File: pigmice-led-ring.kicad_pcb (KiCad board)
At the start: 2 copper layers, 46 x 51 mm, 46 parts, among them J1 Conn_01x02_Female, J2 Conn_01x03_Female, U1 LMR62014XMF

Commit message: Cleanup voltage regulator circuit spacing
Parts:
- moved C1 1.38 mm to (78.6, 99.3)
- moved CF1 1.34 mm to (79.6, 105.8)
- moved U1 1.18 mm to (78.8, 102.0)
- moved C2 1.17 mm to (75.2, 103.6)
- moved R2 1.15 mm to (81.6, 105.2)
- moved R3 1.13 mm to (81.6, 101.8)
- moved D1 1.11 mm to (74.5, 101.5)
- moved R1 1.11 mm to (77.8, 105.8)
- moved L1 0.40 mm to (74.6, 98.2)
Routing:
- net GND: track 17.7 -> 8.85 mm
- net /Vled: track 10.3 -> 7.52 mm
- net /PWM: track 15.3 -> 16.4 mm
- net Net-(D1-Pad2): track 7.42 -> 6.85 mm

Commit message: Add sponsor logos
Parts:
- added G***: LOGO, led-ring:oshpark_logo, B.Cu at (84.0, 99.5)
- added G***: LOGO, led-ring:terrazign_logo, B.Cu at (107.0, 70.5)
- added G***: LOGO, led-ring:daimler_logo, B.Cu at (79.0, 60.0)
- added G***: LOGO, led-ring:flir_logo, B.Cu at (102.0, 61.0)
- added G***: LOGO, led-ring:frc_logo, B.Cu at (90.0, 62.0)
- added G***: LOGO, led-ring:o_edu_logo, B.Cu at (108.0, 80.0)
- added G***: LOGO, led-ring:oshw_logo, B.Cu at (96.5, 99.0)
- added G***: LOGO, led-ring:sw_logo, B.Cu at (76.5, 65.0)
- added G***: LOGO, led-ring:urs_electronics_logo, B.Cu at (72.0, 80.0)
- added G***: LOGO, led-ring:dw_fritz_logo, B.Cu at (107.0, 89.0)
- added G***: LOGO, led-ring:true_value_logo, B.Cu at (73.0, 89.0)
- added G***: LOGO, led-ring:boeing_logo, B.Cu at (73.0, 70.0)
- added G***: LOGO, led-ring:te_logo, B.Cu at (104.0, 65.0)

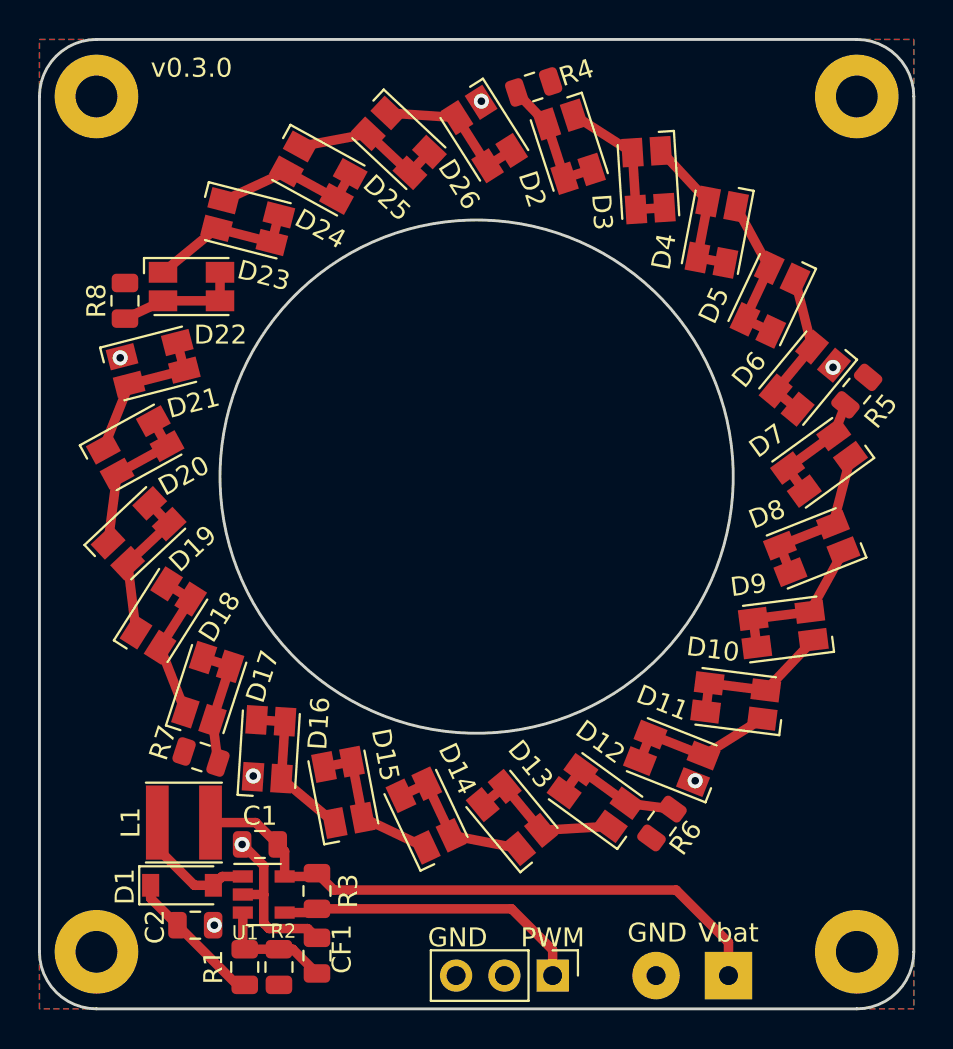
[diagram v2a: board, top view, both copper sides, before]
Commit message: Move LED vias out of underneath pad
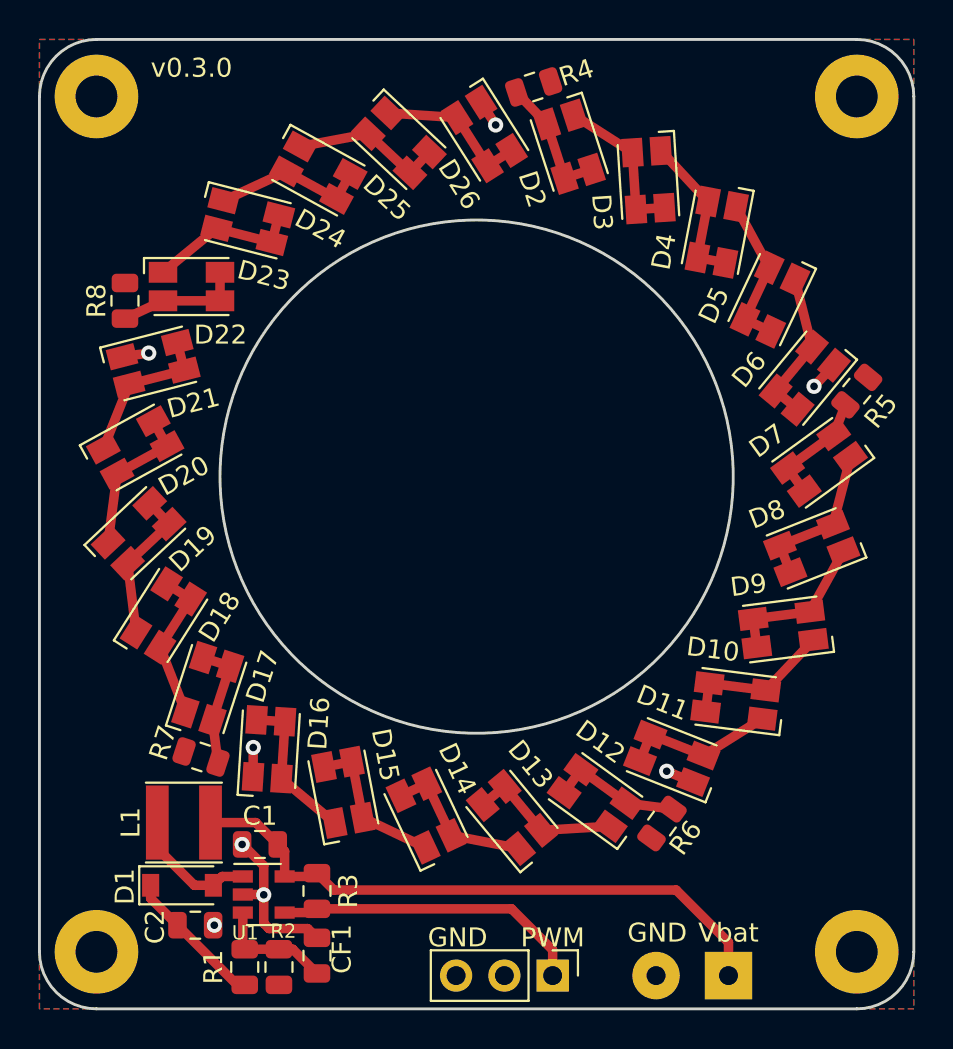
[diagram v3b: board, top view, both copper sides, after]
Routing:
- net GND: track 8.85 -> 16.3 mm, vias 7 -> 8
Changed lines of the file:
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@@
     (thickness 1.6)
     (drawings 14)
-    (tracks 122)
+    (tracks 132)
     (zones 0)
     (modules 59)
@@
     (34 B.Paste user)
     (35 F.Paste user)
-    (36 B.SilkS user)
+    (36 B.SilkS user hide)
     (37 F.SilkS user)
     (38 B.Mask user)
@@
     (via_min_size 0.4)
     (via_min_drill 0.3)
+    (user_via 0.6 0.3)
     (uvia_size 0.3)
     (uvia_drill 0.1)
@@
   (gr_arc (start 110 60) (end 113 60) (angle -90) (layer Edge.Cuts) (width 0.15))
   (gr_arc (start 70 60) (end 70 57) (angle -90) (layer Edge.Cuts) (width 0.15))
+  (via (at 76.2 103.6) (size 0.8) (drill 0.4) (layers F.Cu B.Cu) (net 2))
   (segment (start 81.402661 102.934839) (end 81.6 102.7375) (width 0.5) (layer F.Cu) (net 1))
   (segment (start 79.9 102.934839) (end 81.402661 102.934839) (width 0.5) (layer F.Cu) (net 1))
@@
   (segment (start 91.8375 102.7375) (end 81.6 102.7375) (width 0.5) (layer F.Cu) (net 1))
   (segment (start 94 104.9) (end 91.8375 102.7375) (width 0.5) (layer F.Cu) (net 1))
-  (via (at 76.2 103.6) (size 0.8) (drill 0.4) (layers F.Cu B.Cu) (net 2))
-  (via (at 78.25 95.75) (size 0.8) (drill 0.4) (layers F.Cu B.Cu) (net 2))
-  (via (at 108.75 74.25) (size 0.8) (drill 0.4) (layers F.Cu B.Cu) (net 2))
-  (via (at 101.5 96) (size 0.8) (drill 0.4) (layers F.Cu B.Cu) (net 2))
-  (via (at 71.25 73.75) (size 0.8) (drill 0.4) (layers F.Cu B.Cu) (net 2))
-  (via (at 90.25 60.25) (size 0.8) (drill 0.4) (layers F.Cu B.Cu) (net 2))
+  (via (at 78.25 94.25) (size 0.8) (drill 0.4) (layers F.Cu B.Cu) (net 2))
+  (via (at 107.75 75.25) (size 0.8) (drill 0.4) (layers F.Cu B.Cu) (net 2))
+  (via (at 100 95.5) (size 0.8) (drill 0.4) (layers F.Cu B.Cu) (net 2))
+  (via (at 72.75 73.5) (size 0.8) (drill 0.4) (layers F.Cu B.Cu) (net 2))
+  (via (at 91 61.5) (size 0.8) (drill 0.4) (layers F.Cu B.Cu) (net 2))
   (segment (start 77.680163 99.35) (end 78.8 100.469837) (width 0.5) (layer F.Cu) (net 2))
   (segment (start 77.6625 99.35) (end 77.6625 99.35) (width 0.5) (layer F.Cu) (net 2))
@@
   (segment (start 81.114473 103.776973) (end 81.6 104.2625) (width 0.5) (layer F.Cu) (net 2))
   (segment (start 78.8 103.499841) (end 79.077132 103.776973) (width 0.5) (layer F.Cu) (net 2))
+  (segment (start 78.8 102) (end 78.8 102) (width 0.5) (layer F.Cu) (net 2))
+  (segment (start 77.6625 99.35) (end 77.6625 99.35) (width 0.5) (layer F.Cu) (net 2))
+  (segment (start 91 61.5) (end 90.235383 60.308451) (width 0.5) (layer F.Cu) (net 2))
+  (segment (start 107.75 75.25) (end 108.800513 74.138839) (width 0.5) (layer F.Cu) (net 2))
+  (segment (start 100 95.5) (end 101.383973 96.069152) (width 0.5) (layer F.Cu) (net 2))
+  (segment (start 78.25 94.25) (end 78.235169 95.792443) (width 0.5) (layer F.Cu) (net 2))
+  (segment (start 72.75 73.5) (end 71.344962 73.691114) (width 0.5) (layer F.Cu) (net 2))
+  (segment (start 78.8 102) (end 78.8 102) (width 0.5) (layer F.Cu) (net 2))
+  (segment (start 78.8 102) (end 78.8 102) (width 0.5) (layer F.Cu) (net 2))
   (segment (start 78.8 102) (end 78.8 103.499841) (width 0.5) (layer F.Cu) (net 2))
+  (via (at 78.8 102) (size 0.8) (drill 0.4) (layers F.Cu B.Cu) (net 2))
   (segment (start 77.6625 99.35) (end 77.680163 99.35) (width 0.5) (layer F.Cu) (net 2))
   (via (at 77.6625 99.35) (size 0.8) (drill 0.4) (layers F.Cu B.Cu) (net 2))
@@
   (segment (start 103.25 104.50032) (end 100.49968 101.75) (width 0.5) (layer F.Cu) (net 12))
   (segment (start 103.25 106.25) (end 103.25 104.50032) (width 0.5) (layer F.Cu) (net 12))
-  (segment (start 78.3875 98.2) (end 79.5375 99.35) (width 0.5) (layer F.Cu) (net 12))
-  (segment (start 76 98.2) (end 78.3875 98.2) (width 0.5) (layer F.Cu) (net 12))
   (segment (start 79.9 99.7125) (end 79.5375 99.35) (width 0.5) (layer F.Cu) (net 12))
   (segment (start 79.9 101.034839) (end 79.9 99.7125) (width 0.5) (layer F.Cu) (net 12))
@@
   (segment (start 82.4875 101.75) (end 100.49968 101.75) (width 0.5) (layer F.Cu) (net 12))
   (segment (start 81.6 100.8625) (end 82.4875 101.75) (width 0.5) (layer F.Cu) (net 12))
+  (segment (start 78.3875 98.2) (end 79.5375 99.35) (width 0.5) (layer F.Cu) (net 12))
+  (segment (start 76 98.2) (end 78.3875 98.2) (width 0.5) (layer F.Cu) (net 12))
   (segment (start 103.089234 68.753471) (end 101.615805 68.472399) (width 0.5) (layer F.Cu) (net 14))
   (segment (start 101.615805 68.472399) (end 102.17795 65.525537) (width 0.5) (layer F.Cu) (net 14))

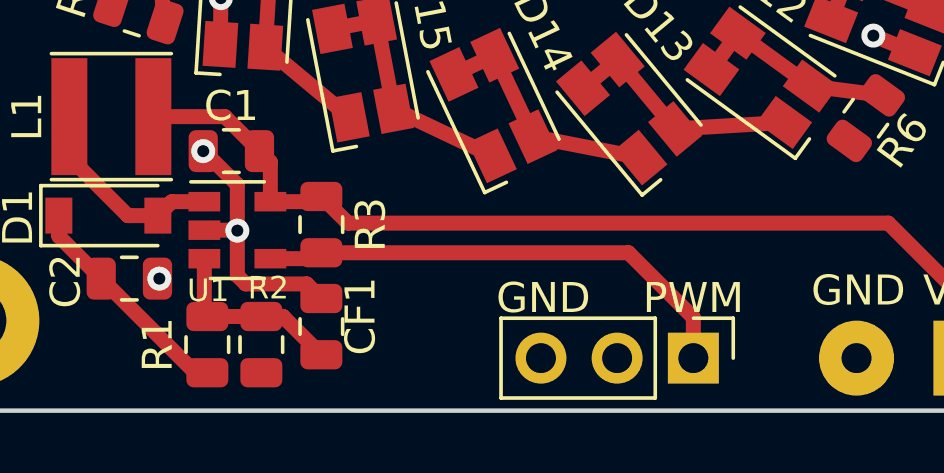
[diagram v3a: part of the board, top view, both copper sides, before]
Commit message: Fix R2/CF1 labels
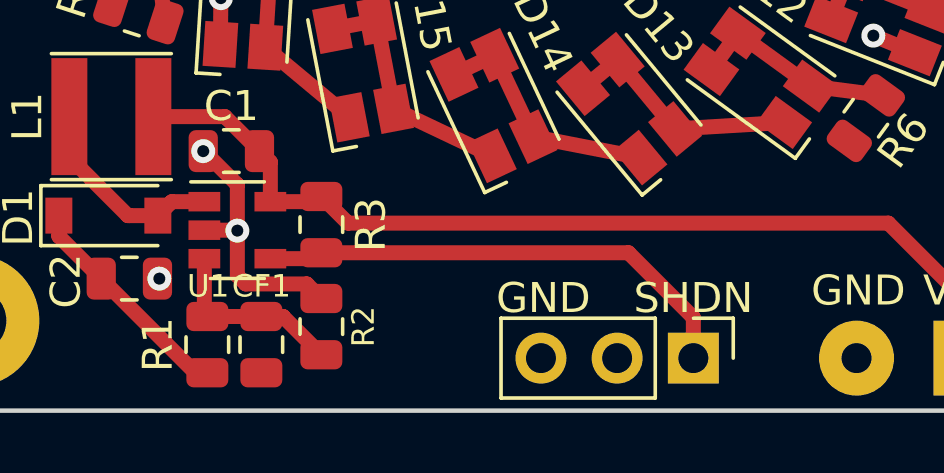
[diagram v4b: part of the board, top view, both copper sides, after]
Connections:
- net /PWM renamed /SHDN
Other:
- board text added: "SHDN"
- board text removed: "PWM"

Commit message: Center URS logo better
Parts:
- moved G*** 0.25 mm to (71.8, 80.0)
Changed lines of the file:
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@@
     (34 B.Paste user)
     (35 F.Paste user)
-    (36 B.SilkS user hide)
+    (36 B.SilkS user)
     (37 F.SilkS user)
     (38 B.Mask user)
@@
   )
   (module led-ring:urs_electronics_logo (layer B.Cu)
-    (at 72 80 180)
+    (at 71.75 80 180)
     (fp_text reference G*** (at 0 0) (layer B.SilkS) hide
       (effects (font (size 1.524 1.524) (thickness 0.3)) (justify mirror))
@@
   (gr_arc (start 110 60) (end 113 60) (angle -90) (layer Edge.Cuts) (width 0.15))
   (gr_arc (start 70 60) (end 70 57) (angle -90) (layer Edge.Cuts) (width 0.15))
-  (segment (start 81.402661 102.934839) (end 81.6 102.7375) (width 0.5) (layer F.Cu) (net 32))
-  (segment (start 79.9 102.934839) (end 81.402661 102.934839) (width 0.5) (layer F.Cu) (net 32))
-  (segment (start 94 106.25) (end 94 104.9) (width 0.5) (layer F.Cu) (net 32))
-  (segment (start 91.8375 102.7375) (end 81.6 102.7375) (width 0.5) (layer F.Cu) (net 32))
-  (segment (start 94 104.9) (end 91.8375 102.7375) (width 0.5) (layer F.Cu) (net 32))
   (via (at 76.2 103.6) (size 0.8) (drill 0.4) (layers F.Cu B.Cu) (net 1))
   (via (at 78.25 94.25) (size 0.8) (drill 0.4) (layers F.Cu B.Cu) (net 1))
@@
   (segment (start 85.330899 60.86856) (end 88.968892 61.112191) (width 0.5) (layer F.Cu) (net 31))
   (segment (start 90.576371 63.645175) (end 88.968892 61.112191) (width 0.5) (layer F.Cu) (net 31))
+  (segment (start 81.402661 102.934839) (end 81.6 102.7375) (width 0.5) (layer F.Cu) (net 32))
+  (segment (start 79.9 102.934839) (end 81.402661 102.934839) (width 0.5) (layer F.Cu) (net 32))
+  (segment (start 94 106.25) (end 94 104.9) (width 0.5) (layer F.Cu) (net 32))
+  (segment (start 91.8375 102.7375) (end 81.6 102.7375) (width 0.5) (layer F.Cu) (net 32))
+  (segment (start 94 104.9) (end 91.8375 102.7375) (width 0.5) (layer F.Cu) (net 32))
   (zone (net 1) (net_name GND) (layer B.Cu) (hatch edge 0.508)
     (connect_pads (clearance 0.508))

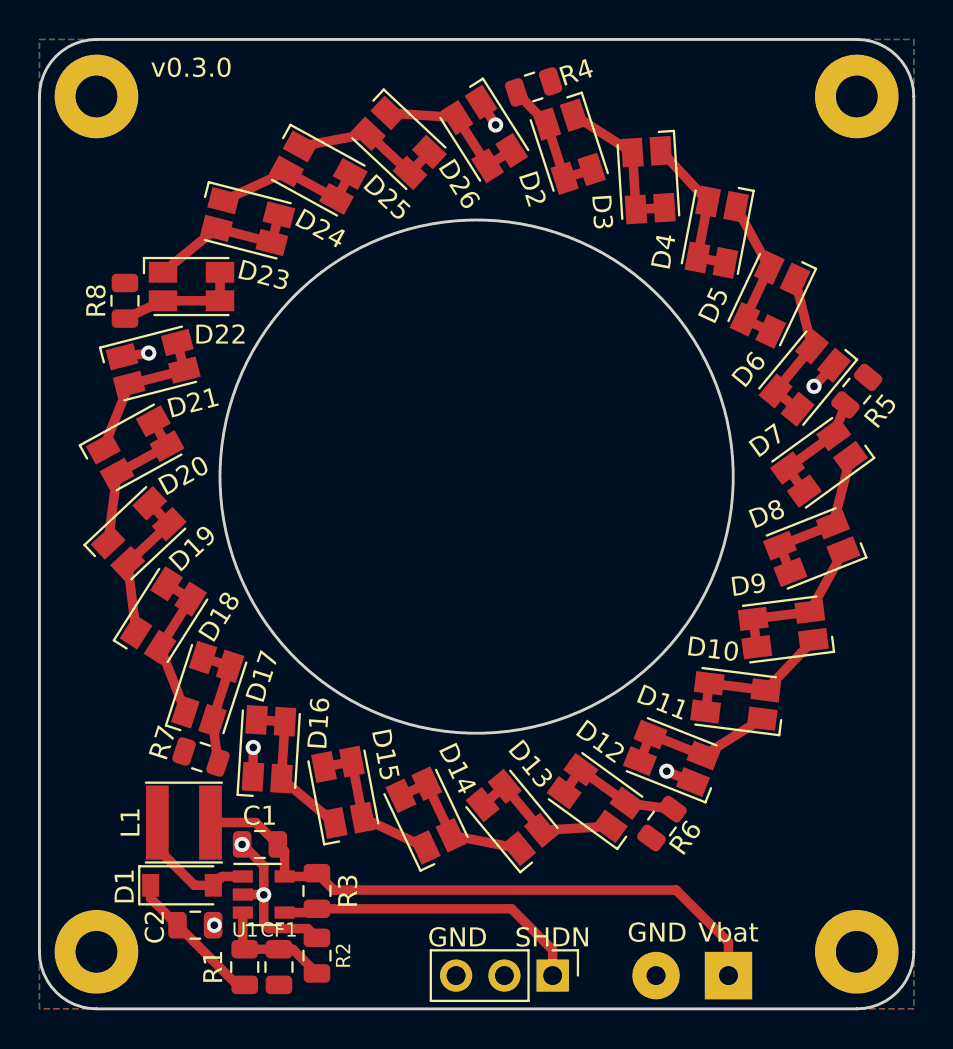
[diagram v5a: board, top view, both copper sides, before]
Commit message: Swap out inductor for smaller 2410 footprint
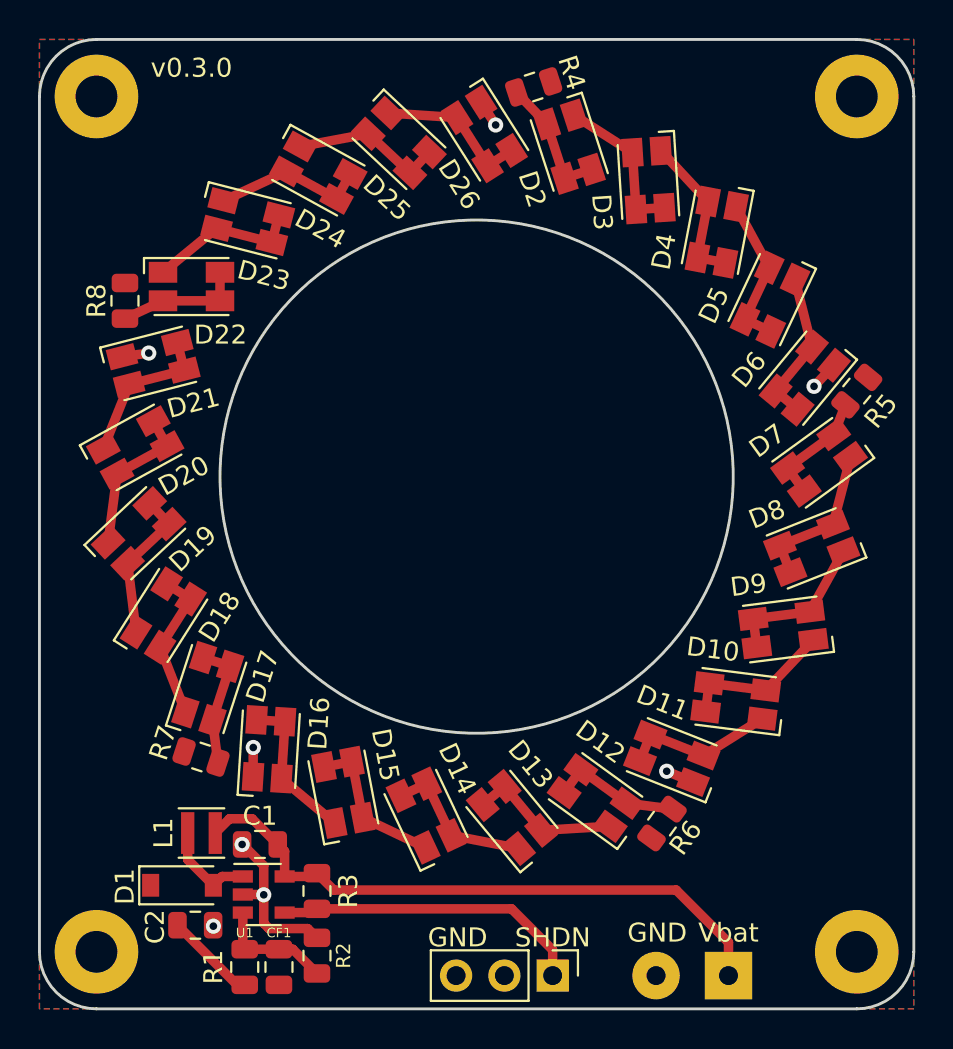
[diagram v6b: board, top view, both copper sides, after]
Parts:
- L1: footprint Inductor_SMD:L_Taiyo-Yuden_NR-40xx -> Inductor_SMD:L_Taiyo-Yuden_NR-24xx
- moved L1 1.08 mm to (75.5, 98.8)
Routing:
- net /Vled: track 7.52 -> 4.84 mm
- net Net-(D1-Pad2): track 6.85 -> 5.05 mm

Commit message: Switch from 150 to 137 ohm resistors for LEDs
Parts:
- R4, R5, R6, R7, R8: value 150Ω -> 137Ω
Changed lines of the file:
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@@
       (effects (font (size 1 1) (thickness 0.15)))
     )
-    (fp_text value 150Ω (at 0 1.65 90) (layer F.Fab)
+    (fp_text value 137Ω (at 0 1.65 90) (layer F.Fab)
       (effects (font (size 1 1) (thickness 0.15)))
     )
@@
       (effects (font (size 1 1) (thickness 0.15)))
     )
-    (fp_text value 150Ω (at 0 1.65 54) (layer F.Fab)
+    (fp_text value 137Ω (at 0 1.65 54) (layer F.Fab)
       (effects (font (size 1 1) (thickness 0.15)))
     )
@@
       (effects (font (size 1 1) (thickness 0.15)))
     )
-    (fp_text value 150Ω (at 0 1.65 162) (layer F.Fab)
+    (fp_text value 137Ω (at 0 1.65 162) (layer F.Fab)
       (effects (font (size 1 1) (thickness 0.15)))
     )
@@
       (effects (font (size 1 1) (thickness 0.15)))
     )
-    (fp_text value 150Ω (at 0 1.65 18) (layer F.Fab)
+    (fp_text value 137Ω (at 0 1.65 18) (layer F.Fab)
       (effects (font (size 1 1) (thickness 0.15)))
     )
@@
       (effects (font (size 1 1) (thickness 0.15)))
     )
-    (fp_text value 150Ω (at 0 1.65 50.4) (layer F.Fab)
-      (effects (font (size 1 1) (thickness 0.15)))
-    )
+    (fp_text value 137Ω (at 0 1.65 50.4) (layer F.Fab)
+      (effects (font (size 1 1) (thickness 0.15)))
+    )
